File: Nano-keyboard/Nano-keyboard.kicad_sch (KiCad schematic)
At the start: 40 parts, among them J1 125SH-B-04-TS, J2 125SH-B-02-TS, U1 AMS1117, U2 ESP32-WROOM-32, U3 J5019, U5 EN12-HN22AF25, U6 EN12-HN22AF25

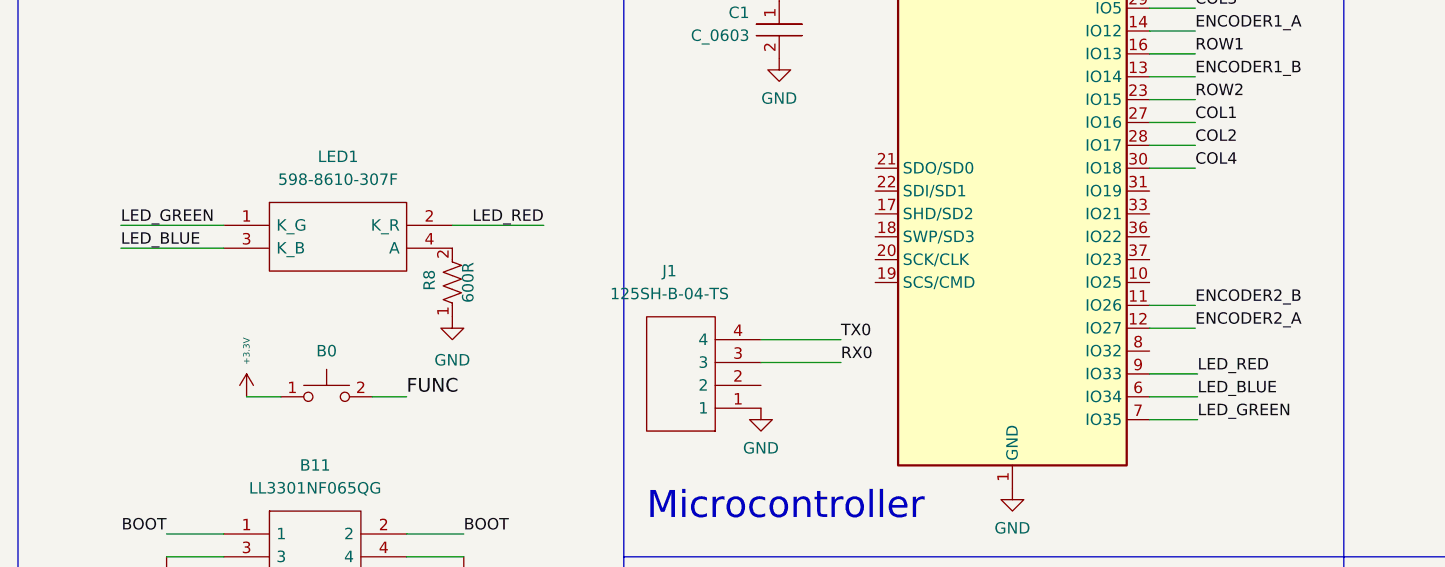
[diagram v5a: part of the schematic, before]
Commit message: Added RGB leds
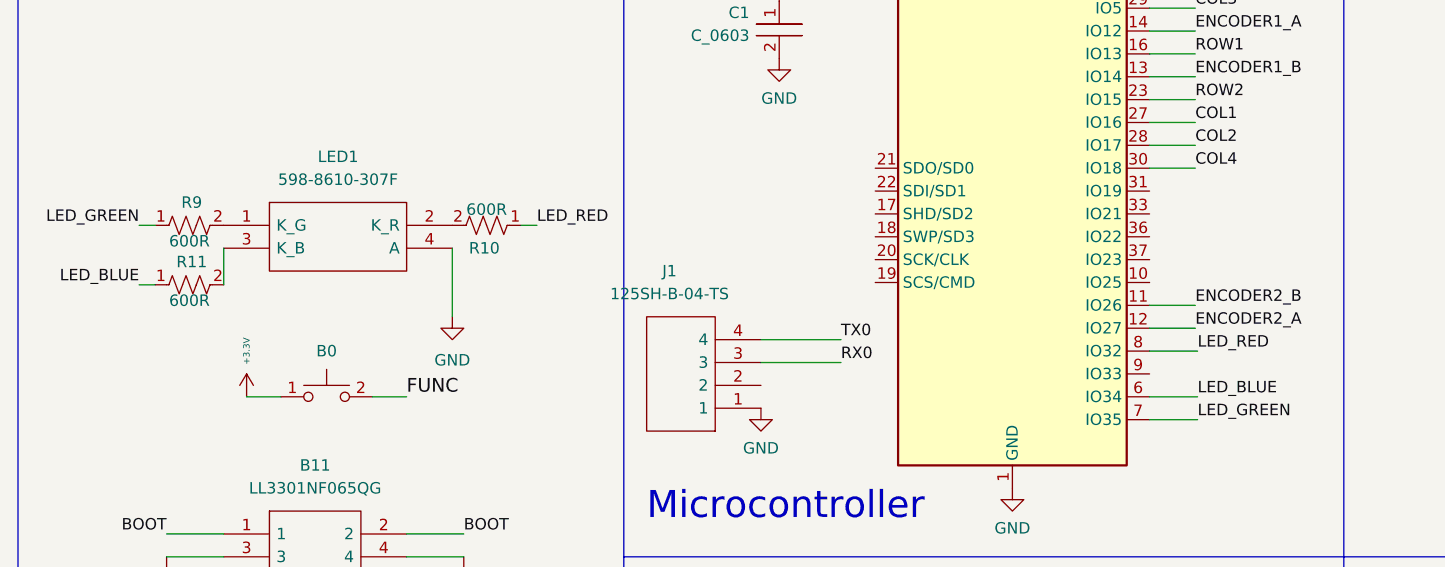
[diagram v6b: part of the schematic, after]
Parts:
- removed R8: R_0603, lib:R_0603_1608Metric, symbol custom-keyboard:R_0603
- added R10, R11, R9: R_0603, lib:R_0603_1608Metric, symbol custom-keyboard:R_0603
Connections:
- net GND: now also LED1.4 (A)
- net LED_BLUE: now also R11.1; no longer LED1.3 (K_B)
- net LED_GREEN: now also R9.1; no longer LED1.1 (K_G)
- net LED_RED: now also U2.8 (IO32), R10.1; no longer LED1.2 (K_R), U2.9 (IO33)
- new net: LED1.2 (K_R), R10.2
- new net: LED1.1 (K_G), R9.2
- new net: LED1.3 (K_B), R11.2
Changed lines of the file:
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@@
+    (stroke (width 0) (type default) (color 0 0 0 0))
+  )
+  (wire (pts (xy 53.34 89.154) (xy 53.34 85.09))
     (stroke (width 0) (type default) (color 0 0 0 0))
   )
@@
     (stroke (width 0) (type default) (color 0 0 0 0))
   )
-  (wire (pts (xy 41.91 85.09) (xy 53.34 85.09))
-    (stroke (width 0) (type default) (color 0 0 0 0))
-  )
   (polyline (pts (xy 177.8 119.38) (xy 97.79 119.38))
     (stroke (width 0) (type default) (color 0 0 0 0))
@@
     (stroke (width 0) (type default) (color 0 0 0 0))
   )
+  (wire (pts (xy 45.72 82.55) (xy 43.942 82.55))
+    (stroke (width 0) (type default) (color 0 0 0 0))
+  )
   (wire (pts (xy 237.49 71.12) (xy 245.11 71.12))
     (stroke (width 0) (type default) (color 0 0 0 0))
@@
     (stroke (width 0) (type default) (color 0 0 0 0))
   )
-  (wire (pts (xy 156.21 99.06) (xy 161.544 99.06))
-    (stroke (width 0) (type default) (color 0 0 0 0))
-  )
   (wire (pts (xy 161.29 93.98) (xy 156.21 93.98))
     (stroke (width 0) (type default) (color 0 0 0 0))
@@
     (stroke (width 0) (type default) (color 0 0 0 0))
   )
+  (wire (pts (xy 45.72 89.154) (xy 43.942 89.154))
+    (stroke (width 0) (type default) (color 0 0 0 0))
+  )
   (wire (pts (xy 118.11 50.8) (xy 114.3 50.8))
     (stroke (width 0) (type default) (color 0 0 0 0))
@@
     (stroke (width 0) (type default) (color 0 0 0 0))
   )
-  (wire (pts (xy 41.91 82.55) (xy 53.34 82.55))
-    (stroke (width 0) (type default) (color 0 0 0 0))
-  )
   (wire (pts (xy 161.29 60.96) (xy 156.21 60.96))
     (stroke (width 0) (type default) (color 0 0 0 0))
@@
     (stroke (width 0) (type default) (color 0 0 0 0))
   )
+  (wire (pts (xy 86.36 82.55) (xy 88.138 82.55))
+    (stroke (width 0) (type default) (color 0 0 0 0))
+  )
+  (wire (pts (xy 156.21 96.52) (xy 161.544 96.52))
+    (stroke (width 0) (type default) (color 0 0 0 0))
+  )
   (wire (pts (xy 168.148 143.51) (xy 168.148 138.43))
     (stroke (width 0) (type default) (color 0 0 0 0))
@@
     (stroke (width 0) (type default) (color 0 0 0 0))
   )
-  (wire (pts (xy 78.74 82.55) (xy 88.9 82.55))
+  (wire (pts (xy 78.74 85.09) (xy 78.74 92.71))
     (stroke (width 0) (type default) (color 0 0 0 0))
   )
@@
     (effects (font (size 1.27 1.27)) (justify left bottom))
   )
-  (label "LED_BLUE" (at 41.91 85.09 0)
-    (effects (font (size 1.27 1.27)) (justify left bottom))
+  (label "LED_GREEN" (at 43.942 82.55 180)
+    (effects (font (size 1.27 1.27)) (justify right bottom))
   )
   (label "ROW1" (at 200.66 71.12 0)
+    (effects (font (size 1.27 1.27)) (justify left bottom))
+  )
+  (label "LED_RED" (at 161.544 96.52 0)
     (effects (font (size 1.27 1.27)) (justify left bottom))
   )
@@
     (effects (font (size 1.524 1.524)) (justify left bottom))
   )
-  (label "LED_RED" (at 88.9 82.55 180)
-    (effects (font (size 1.27 1.27)) (justify right bottom))
-  )
   (label "TX0" (at 161.29 48.26 0)
     (effects (font (size 1.27 1.27)) (justify left bottom))
@@
     (effects (font (size 1.27 1.27)) (justify right bottom))
   )
-  (label "LED_RED" (at 161.544 99.06 0)
-    (effects (font (size 1.27 1.27)) (justify left bottom))
-  )
   (label "LED_BLUE" (at 161.544 101.6 0)
-    (effects (font (size 1.27 1.27)) (justify left bottom))
-  )
-  (label "LED_GREEN" (at 41.91 82.55 0)
     (effects (font (size 1.27 1.27)) (justify left bottom))
   )
@@
     (effects (font (size 1.27 1.27)) (justify left bottom))
   )
+  (label "LED_RED" (at 88.138 82.55 0)
+    (effects (font (size 1.27 1.27)) (justify left bottom))
+  )
   (label "ROW3" (at 200.66 114.3 0)
     (effects (font (size 1.27 1.27)) (justify left bottom))
@@
   (label "RX0" (at 121.92 97.79 0)
     (effects (font (size 1.27 1.27)) (justify left bottom))
+  )
+  (label "LED_BLUE" (at 43.942 89.154 180)
+    (effects (font (size 1.27 1.27)) (justify right bottom))
   )
   (global_label "COL4" (shape input) (at 248.92 46.99 90) (fields_autoplaced)
@@
     )
     (property "Capacitance" "" (id 4) (at 115.062 61.468 0)
+      (effects (font (size 1.27 1.27)) (justify bottom))
+    )
+    (pin "1")
+    (pin "2")
+  )
+  (symbol (lib_id "custom-keyboard:R_0603") (at 82.804 82.55 270) (unit 1)
+    (in_bom yes) (on_board yes)
+    (property "Reference" "R10" (id 0) (at 82.296 85.09 90))
+    (property "Value" "R_0603" (id 1) (at 82.55 86.233 90)
+      (effects (font (size 1.27 1.27)) hide)
+    )
+    (property "Footprint" "lib:R_0603_1608Metric" (id 2) (at 82.804 82.55 0)
+      (effects (font (size 1.27 1.27)) hide)
+    )
+    (property "Datasheet" "" (id 3) (at 82.804 82.55 0)
+      (effects (font (size 1.27 1.27)) hide)
+    )
+    (property "Resistance" "600R" (id 4) (at 82.55 81.534 90)
       (effects (font (size 1.27 1.27)) (justify bottom))
     )
@@
     (pin "2")
   )
-  (symbol (lib_id "custom-keyboard:R_0603") (at 78.74 89.154 180) (unit 1)
-    (in_bom yes) (on_board yes)
-    (property "Reference" "R8" (id 0) (at 76.2 88.646 90))
-    (property "Value" "R_0603" (id 1) (at 75.057 88.9 90)
-      (effects (font (size 1.27 1.27)) hide)
-    )
-    (property "Footprint" "lib:R_0603_1608Metric" (id 2) (at 78.74 89.154 0)
-      (effects (font (size 1.27 1.27)) hide)
-    )
-    (property "Datasheet" "" (id 3) (at 78.74 89.154 0)
-      (effects (font (size 1.27 1.27)) hide)
-    )
-    (property "Resistance" "600R" (id 4) (at 79.756 88.9 90)
-      (effects (font (size 1.27 1.27)) (justify bottom))
-    )
-    (pin "1")
-    (pin "2")
-  )
   (symbol (lib_id "power:GND") (at 145.288 144.78 0) (unit 1)
     (in_bom yes) (on_board yes) (fields_autoplaced)
@@
     )
     (pin "1")
+  )
+  (symbol (lib_id "custom-keyboard:R_0603") (at 49.276 82.55 90) (unit 1)
+    (in_bom yes) (on_board yes)
+    (property "Reference" "R9" (id 0) (at 49.784 80.01 90))
+    (property "Value" "R_0603" (id 1) (at 49.53 78.867 90)
+      (effects (font (size 1.27 1.27)) hide)
+    )
+    (property "Footprint" "lib:R_0603_1608Metric" (id 2) (at 49.276 82.55 0)
+      (effects (font (size 1.27 1.27)) hide)
+    )
+    (property "Datasheet" "" (id 3) (at 49.276 82.55 0)
+      (effects (font (size 1.27 1.27)) hide)
+    )
+    (property "Resistance" "600R" (id 4) (at 49.53 83.566 90)
+      (effects (font (size 1.27 1.27)) (justify bottom))
+    )
+    (pin "1")
+    (pin "2")
   )
   (symbol (lib_id "custom-keyboard:R_0603") (at 187.198 137.668 270) (unit 1)
@@
     )
     (pin "1")
+  )
+  (symbol (lib_id "custom-keyboard:R_0603") (at 49.276 89.154 90) (unit 1)
+    (in_bom yes) (on_board yes)
+    (property "Reference" "R11" (id 0) (at 49.784 86.614 90))
+    (property "Value" "R_0603" (id 1) (at 49.53 85.471 90)
+      (effects (font (size 1.27 1.27)) hide)
+    )
+    (property "Footprint" "lib:R_0603_1608Metric" (id 2) (at 49.276 89.154 0)
+      (effects (font (size 1.27 1.27)) hide)
+    )
+    (property "Datasheet" "" (id 3) (at 49.276 89.154 0)
+      (effects (font (size 1.27 1.27)) hide)
+    )
+    (property "Resistance" "600R" (id 4) (at 49.53 90.17 90)
+      (effects (font (size 1.27 1.27)) (justify bottom))
+    )
+    (pin "1")
+    (pin "2")
   )
   (symbol (lib_id "power:+3.3V") (at 183.134 128.524 0) (unit 1)
@@
       (reference "R7") (unit 1) (value "R_0603") (footprint "lib:R_0603_1608Metric")
     )
-    (path "/94a8a32b-cb10-496b-b880-28e370d2c0b9"
-      (reference "R8") (unit 1) (value "R_0603") (footprint "lib:R_0603_1608Metric")
+    (path "/b5df00ed-108b-4778-8bc0-64bc86e8b2ce"
+      (reference "R9") (unit 1) (value "R_0603") (footprint "lib:R_0603_1608Metric")
+    )
+    (path "/31786174-1573-4ae5-b428-19a2c6370c11"
+      (reference "R10") (unit 1) (value "R_0603") (footprint "lib:R_0603_1608Metric")
+    )
+    (path "/ce9b58af-7b54-4d13-b771-592bf385d86a"
+      (reference "R11") (unit 1) (value "R_0603") (footprint "lib:R_0603_1608Metric")
     )
     (path "/f54960e4-2379-4f0c-bc91-5451a1cb3928"

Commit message: Update
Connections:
- net COL1: now also U2.36 (IO22); no longer U2.27 (IO16)
- net COL2: now also U2.37 (IO23); no longer U2.28 (IO17)
- net COL3: now also U2.27 (IO16); no longer U2.29 (IO5)
- net COL4: now also U2.10 (IO25); no longer U2.30 (IO18)
- net ENCODER1_A: now also U2.28 (IO17); no longer U2.14 (IO12)
- net ENCODER1_B: now also U2.31 (IO19); no longer U2.13 (IO14)
- net ROW1: now also U2.30 (IO18); no longer U2.16 (IO13)
- net ROW2: now also U2.33 (IO21); no longer U2.23 (IO15)
- net ROW3: now also U2.23 (IO15); no longer U2.24 (IO2)
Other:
- title: (none) -> Nano-Keyboard

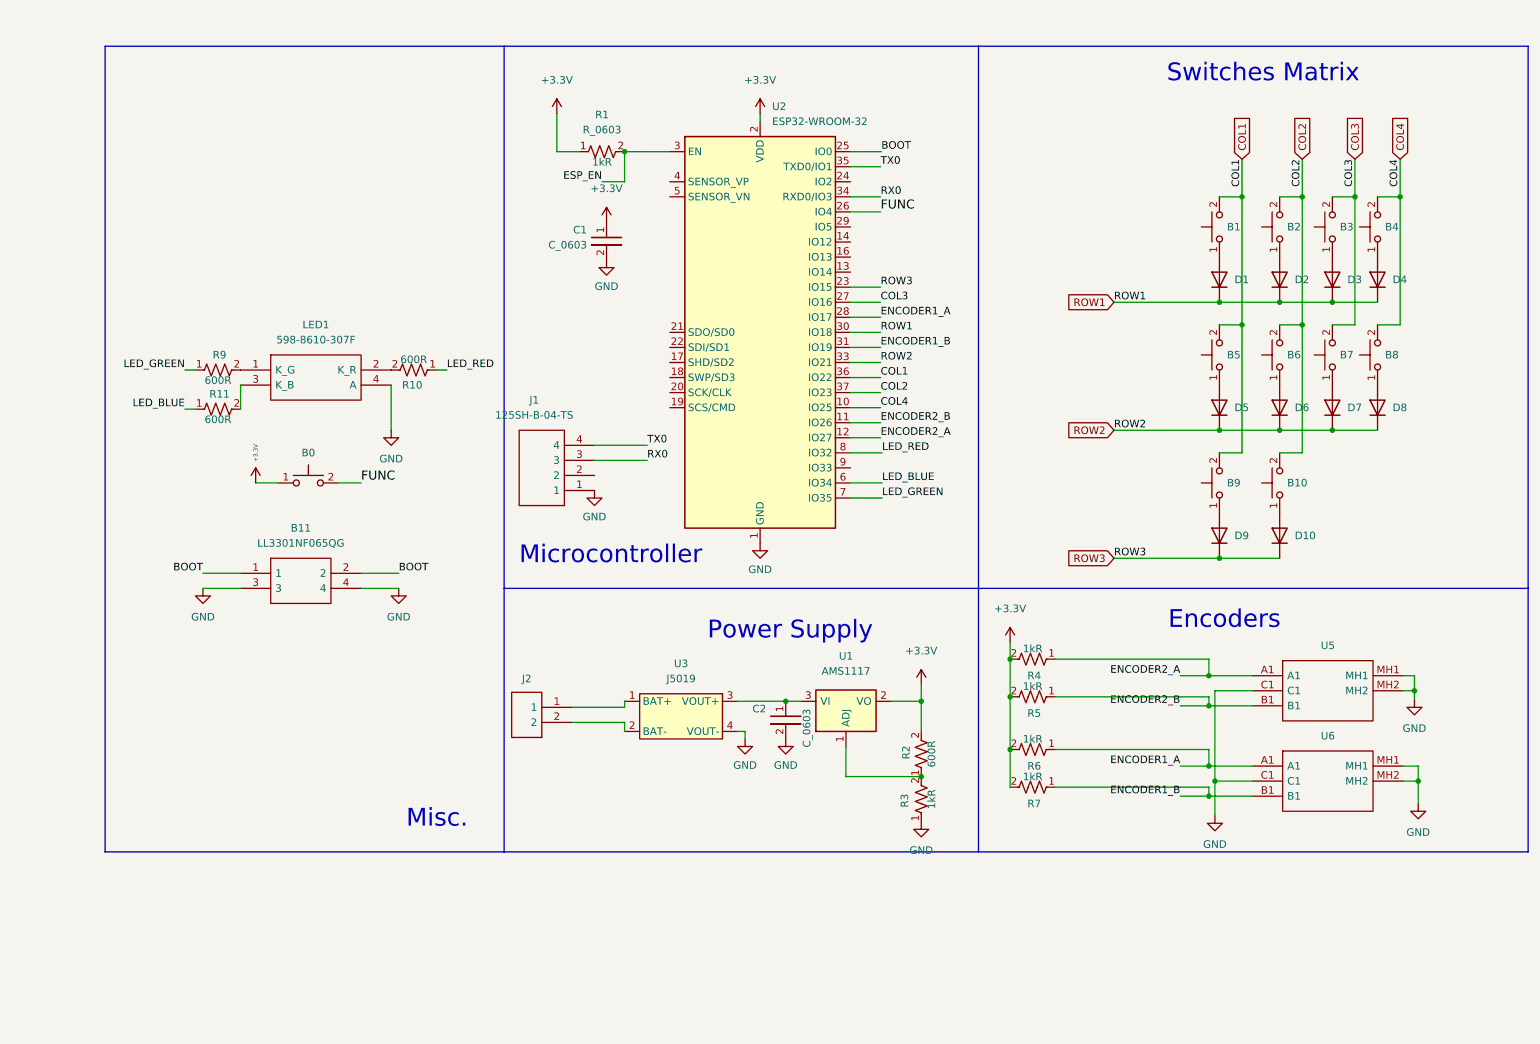
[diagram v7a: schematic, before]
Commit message: added BJTs
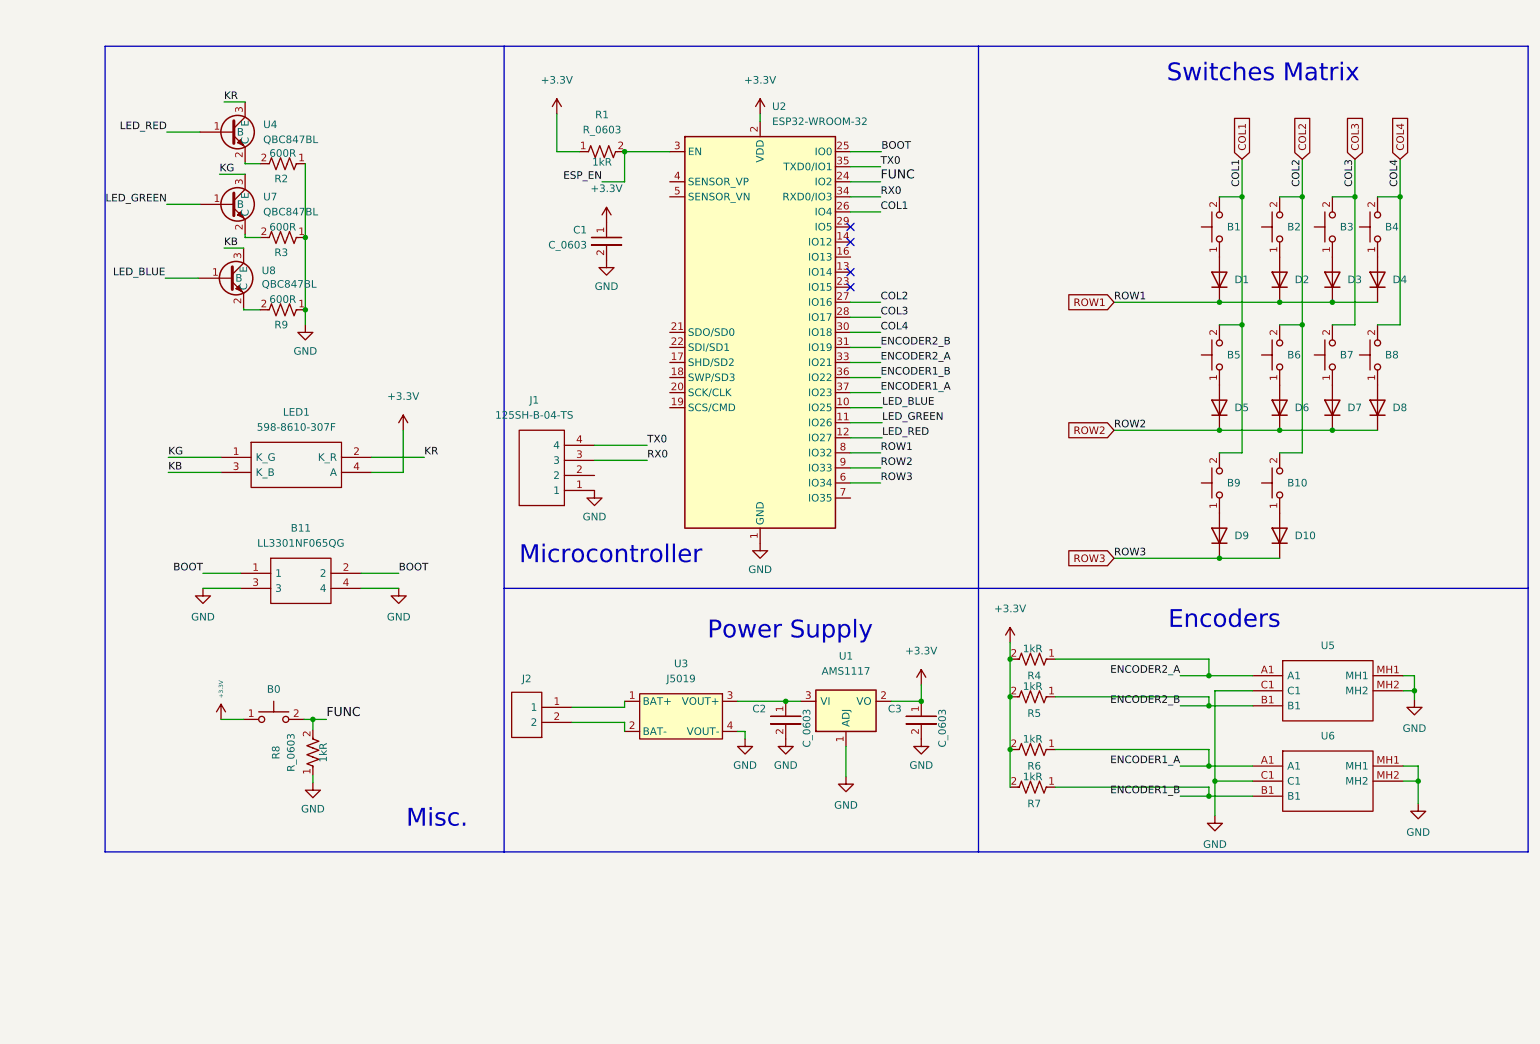
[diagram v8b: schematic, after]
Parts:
- removed R10, R11: R_0603, lib:R_0603_1608Metric, symbol custom-keyboard:R_0603
- added C3: C_0603, lib:C_0603_1608Metric, symbol custom-keyboard:C_0603
- added R8: R_0603, lib:R_0603_1608Metric, symbol custom-keyboard:R_0603
- added U4, U7, U8: QBC847BL, lib:SOT96P237X111-3N, symbol custom-keyboard:QBC847BL
- R3: Resistance 1kR -> 600R
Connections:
- net +3V3: now also LED1.4 (A), C3.1; no longer R2.2
- net COL1: now also U2.26 (IO4); no longer U2.36 (IO22)
- net COL2: now also U2.27 (IO16); no longer U2.37 (IO23)
- net COL3: now also U2.28 (IO17); no longer U2.27 (IO16)
- net COL4: now also U2.30 (IO18); no longer U2.10 (IO25)
- net ENCODER1_A: now also U2.37 (IO23); no longer U2.28 (IO17)
- net ENCODER1_B: now also U2.36 (IO22); no longer U2.31 (IO19)
- net ENCODER2_A: now also U2.33 (IO21); no longer U2.12 (IO27)
- net ENCODER2_B: now also U2.31 (IO19); no longer U2.11 (IO26)
- net FUNC: now also U2.24 (IO2), R8.2; no longer U2.26 (IO4)
- net GND: now also R2.1, R9.1, U1.1 (ADJ), C3.2, R8.1; no longer LED1.4 (A)
- net LED_BLUE: now also U2.10 (IO25), U8.1 (B); no longer U2.6 (IO34)
- net LED_GREEN: now also U2.11 (IO26), U7.1 (B); no longer R9.1, U2.7 (IO35)
- net LED_RED: now also U2.12 (IO27), U4.1 (B); no longer U2.8 (IO32)
- net ROW1: now also U2.8 (IO32); no longer U2.30 (IO18)
- net ROW2: now also U2.9 (IO33); no longer U2.33 (IO21)
- net ROW3: now also U2.6 (IO34); no longer U2.23 (IO15)
- net KR: now reaches LED1.2 (K_R)
- net KR: now also U4.3 (E)
- net at R9.2: now also U8.2 (C); no longer LED1.1 (K_G)
- net KB: now reaches LED1.3 (K_B)
- net KB: now also U8.3 (E)
- new net: R2.2, U4.2 (C)
- new net: R3.2, U7.2 (C)
- new net KG: LED1.1 (K_G), U7.3 (E)
- no-connect marks 0 -> 4
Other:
- moved on the sheet: B0, LED1
